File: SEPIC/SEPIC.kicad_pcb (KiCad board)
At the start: 2 copper layers, 49 x 71.5 mm, 24 parts, among them J1 Screw Terminal, J2 Barrel Jack, J3 Pin Header, J4 Screw Terminal, Q1 IRF520N, U1 HCPL-3120

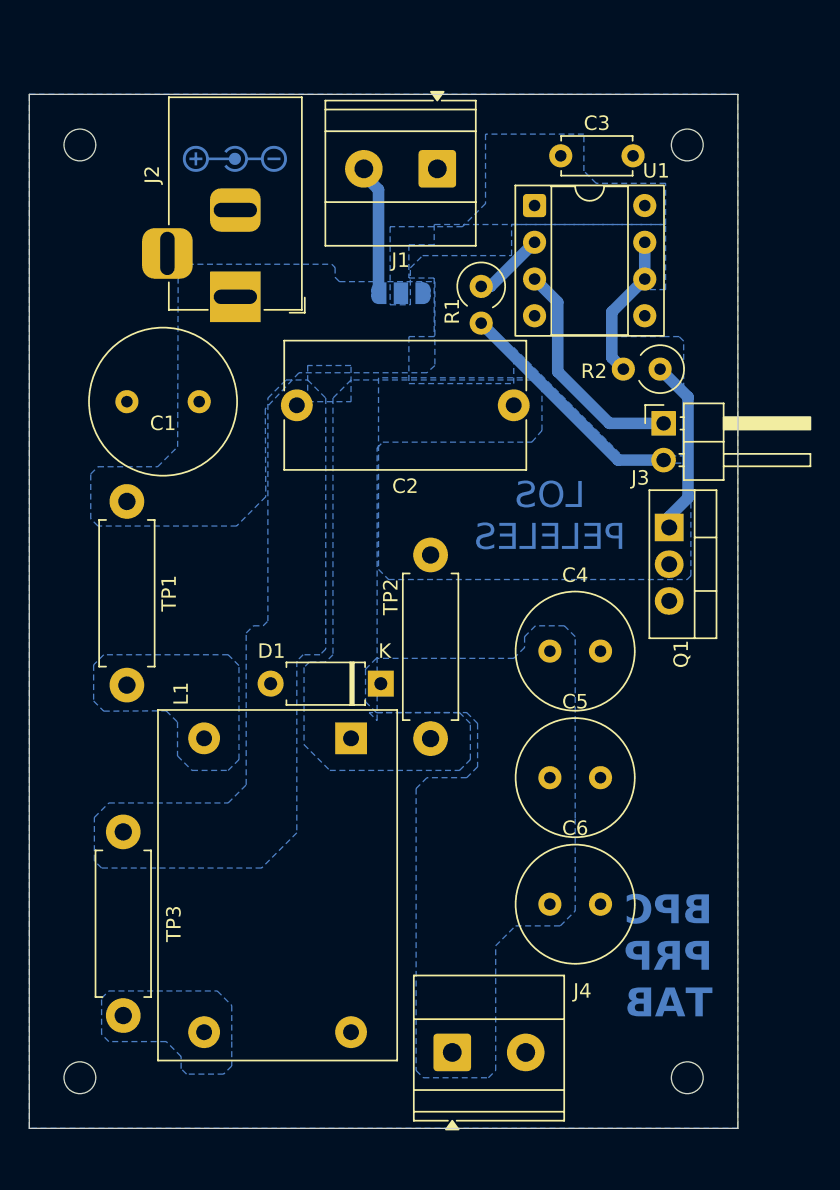
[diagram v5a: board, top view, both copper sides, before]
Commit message: Cambiar tamaño perforaciones
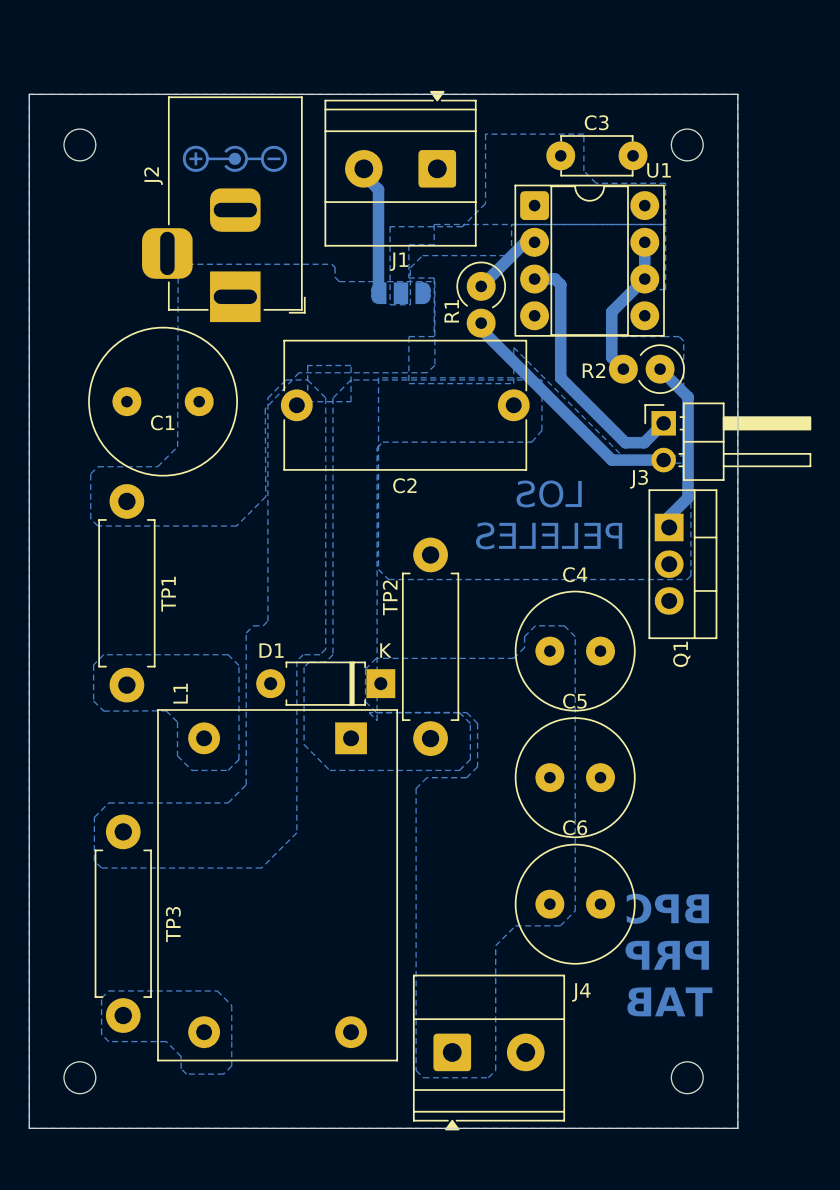
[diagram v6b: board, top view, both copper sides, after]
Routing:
- net Net-(J3-Pin_1): track 15.9 -> 17.9 mm
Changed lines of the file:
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@@
 		(tenting front back)
 		(pcbplotparams
-			(layerselection 0x00000000_00000000_55555555_55555554)
+			(layerselection 0x00000000_00000000_55555555_57555554)
 			(plot_on_all_layers_selection 0x00000000_00000000_00000000_00000000)
 			(disableapertmacros no)
@@
 		(pad "1" thru_hole circle
 			(at 0 0)
-			(size 1.6 1.6)
+			(size 2 2)
 			(drill 0.8)
 			(layers "*.Cu" "*.Mask")
@@
 		(pad "2" thru_hole circle
 			(at 3.5 0)
-			(size 1.6 1.6)
+			(size 2 2)
 			(drill 0.8)
 			(layers "*.Cu" "*.Mask")
@@
 		(pad "1" thru_hole circle
 			(at 0 0)
-			(size 1.6 1.6)
+			(size 2 2)
 			(drill 0.8)
 			(layers "*.Cu" "*.Mask")
@@
 		(pad "2" thru_hole circle
 			(at 3.5 0)
-			(size 1.6 1.6)
+			(size 2 2)
 			(drill 0.8)
 			(layers "*.Cu" "*.Mask")
@@
 		(pad "1" thru_hole circle
 			(at 0 0 180)
-			(size 1.6 1.6)
+			(size 2 2)
 			(drill 0.8)
 			(layers "*.Cu" "*.Mask")
@@
 		(pad "2" thru_hole circle
 			(at 5 0 180)
-			(size 1.6 1.6)
+			(size 2 2)
 			(drill 0.8)
 			(layers "*.Cu" "*.Mask")
@@
 		(pad "1" thru_hole circle
 			(at 0 0 270)
-			(size 1.6 1.6)
+			(size 2 2)
 			(drill 0.8)
 			(layers "*.Cu" "*.Mask")
@@
 			(pintype "passive")
 		)
-		(pad "2" thru_hole oval
+		(pad "2" thru_hole circle
 			(at 2.54 0 270)
-			(size 1.6 1.6)
+			(size 2 2)
 			(drill 0.8)
 			(layers "*.Cu" "*.Mask")
@@
 		(pad "1" thru_hole circle
 			(at 0 0)
-			(size 1.6 1.6)
+			(size 2 2)
 			(drill 0.8)
 			(layers "*.Cu" "*.Mask")
@@
 		(pad "2" thru_hole circle
 			(at 3.5 0)
-			(size 1.6 1.6)
+			(size 2 2)
 			(drill 0.8)
 			(layers "*.Cu" "*.Mask")
@@
 		(pad "1" thru_hole rect
 			(at 0 0 180)
-			(size 1.8 1.8)
+			(size 2 2)
 			(drill 0.9)
 			(layers "*.Cu" "*.Mask")
@@
 			(pintype "passive")
 		)
-		(pad "2" thru_hole oval
+		(pad "2" thru_hole circle
 			(at 7.62 0 180)
-			(size 1.8 1.8)
+			(size 2 2)
 			(drill 0.9)
 			(layers "*.Cu" "*.Mask")
@@
 		(pad "1" thru_hole circle
 			(at 0 0 180)
-			(size 1.6 1.6)
+			(size 2 2)
 			(drill 0.8)
 			(layers "*.Cu" "*.Mask")
@@
 			(pintype "passive")
 		)
-		(pad "2" thru_hole oval
+		(pad "2" thru_hole circle
 			(at 2.54 0 180)
-			(size 1.6 1.6)
+			(size 2 2)
 			(drill 0.8)
 			(layers "*.Cu" "*.Mask")
@@
 		(pad "1" thru_hole circle
 			(at 0 0)
-			(size 1.6 1.6)
+			(size 2 2)
 			(drill 0.8)
 			(layers "*.Cu" "*.Mask")
@@
 		(pad "2" thru_hole circle
 			(at 5 0)
-			(size 1.6 1.6)
+			(size 2 2)
 			(drill 0.8)
 			(layers "*.Cu" "*.Mask")
@@
 		(tags "THT DIP DIL PDIP 2.54mm 7.62mm 300mil Socket")
 		(property "Reference" "U1"
-			(at 8.41 -2.4 0)
+			(at 8.61 -2.4 0)
 			(layer "F.SilkS")
 			(effects
@@
 		(pad "1" thru_hole roundrect
 			(at 0 0)
-			(size 1.6 1.6)
+			(size 2 2)
 			(drill 0.8)
 			(layers "*.Cu" "*.Mask")
@@
 		(pad "2" thru_hole circle
 			(at 0 2.54)
-			(size 1.6 1.6)
+			(size 2 2)
 			(drill 0.8)
 			(layers "*.Cu" "*.Mask")
@@
 		(pad "3" thru_hole circle
 			(at 0 5.08)
-			(size 1.6 1.6)
+			(size 2 2)
 			(drill 0.8)
 			(layers "*.Cu" "*.Mask")
@@
 		(pad "4" thru_hole circle
 			(at 0 7.62)
-			(size 1.6 1.6)
+			(size 2 2)
 			(drill 0.8)
 			(layers "*.Cu" "*.Mask")
@@
 		(pad "5" thru_hole circle
 			(at 7.62 7.62)
-			(size 1.6 1.6)
+			(size 2 2)
 			(drill 0.8)
 			(layers "*.Cu" "*.Mask")
@@
 		(pad "6" thru_hole circle
 			(at 7.62 5.08)
-			(size 1.6 1.6)
+			(size 2 2)
 			(drill 0.8)
 			(layers "*.Cu" "*.Mask")
@@
 		(pad "7" thru_hole circle
 			(at 7.62 2.54)
-			(size 1.6 1.6)
+			(size 2 2)
 			(drill 0.8)
 			(layers "*.Cu" "*.Mask")
@@
 		(pad "8" thru_hole circle
 			(at 7.62 0)
-			(size 1.6 1.6)
+			(size 2 2)
 			(drill 0.8)
 			(layers "*.Cu" "*.Mask")
@@
 	)
 	(segment
-		(start 72.791 40.621)
-		(end 71.19 39.02)
+		(start 73 45.87153)
+		(end 77.46747 50.339)
+		(width 0.8)
+		(layer "B.Cu")
+		(net 10)
+	)
+	(segment
+		(start 71.19 39.02)
+		(end 72.604213 39.02)
+		(width 0.8)
+		(layer "B.Cu")
+		(net 10)
+	)
+	(segment
+		(start 72.604213 39.02)
+		(end 73 39.415787)
 		(width 0.8)
 		(layer "B.Cu")
@@
 	)
 	(segment
-		(start 80.115 49)
-		(end 76.365844 49)
+		(start 77.46747 50.339)
+		(end 78.776 50.339)
 		(width 0.8)
 		(layer "B.Cu")
@@
 	)
 	(segment
-		(start 72.791 45.425156)
-		(end 72.791 40.621)
+		(start 73 39.415787)
+		(end 73 45.87153)
 		(width 0.8)
 		(layer "B.Cu")
@@
 	)
 	(segment
-		(start 76.365844 49)
-		(end 72.791 45.425156)
+		(start 78.776 50.339)
+		(end 80.115 49)
 		(width 0.8)
 		(layer "B.Cu")
@@
 	)
 	(segment
-		(start 76.97 51.54)
+		(start 76.54 51.54)
 		(end 80.115 51.54)
 		(width 0.8)
@@
 	(segment
 		(start 67.5 42.07)
-		(end 76.97 51.54)
+		(end 67.5 42.5)
+		(width 0.8)
+		(layer "B.Cu")
+		(net 11)
+	)
+	(segment
+		(start 67.5 42.5)
+		(end 76.54 51.54)
 		(width 0.8)
 		(layer "B.Cu")
@@
 	)
 	(segment
-		(start 68.14 39.53)
-		(end 71.19 36.48)
+		(start 71.19 36.48)
+		(end 70.55 36.48)
 		(width 0.8)
 		(layer "B.Cu")
@@
 	)
 	(segment
-		(start 67.5 39.53)
-		(end 68.14 39.53)
+		(start 70.55 36.48)
+		(end 67.5 39.53)
 		(width 0.8)
 		(layer "B.Cu")
@@
 	)
 	(segment
-		(start 76.530001 44.450001)
-		(end 76.530001 41.299999)
+		(start 78.803001 39.02)
+		(end 76.530001 41.293)
 		(width 0.8)
 		(layer "B.Cu")
@@
 	)
 	(segment
-		(start 76.530001 41.299999)
-		(end 78.81 39.02)
+		(start 76.530001 41.293)
+		(end 76.530001 44.450001)
 		(width 0.8)
 		(layer "B.Cu")
@@
 	)
 	(segment
-		(start 77.33 45.25)
-		(end 76.530001 44.450001)
+		(start 78.81 39.02)
+		(end 78.803001 39.02)
+		(width 0.8)
+		(layer "B.Cu")
+		(net 14)
+	)
+	(segment
+		(start 76.530001 44.450001)
+		(end 77.33 45.25)
 		(width 0.8)
 		(layer "B.Cu")

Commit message: Imagenes PCB
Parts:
- C3: renamed from C4; value 10u -> 22u
- C4: renamed from C5; footprint Capacitor_THT:C_Radial_D8.0mm_H11.5mm_P3.50mm -> Capacitor_THT:C_Radial_D6.3mm_H7.0mm_P2.50mm
- C5: renamed from C6; value 10u -> 22u
- moved C4 0.75 mm to (73.0, 73.5)
- renumbered C3 to C6
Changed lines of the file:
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@@
 		(descr "C, Radial series, Radial, pin pitch=3.50mm, diameter=8mm, height=11.5mm, Non-Polar Electrolytic Capacitor")
 		(tags "C Radial series Radial pin pitch 3.50mm diameter 8mm height 11.5mm Non-Polar Electrolytic Capacitor")
-		(property "Reference" "C6"
+		(property "Reference" "C5"
 			(at 1.75 -5.25 0)
 			(layer "F.SilkS")
@@
 			)
 		)
-		(property "Value" "10u"
+		(property "Value" "22u"
 			(at 1.75 5.25 0)
 			(layer "F.Fab")
@@
 		)
 	)
-	(footprint "Capacitor_THT:C_Radial_D8.0mm_H11.5mm_P3.50mm"
+	(footprint "Capacitor_THT:C_Radial_D6.3mm_H7.0mm_P2.50mm"
 		(layer "F.Cu")
-		(at 72.25 73.5)
-		(descr "C, Radial series, Radial, pin pitch=3.50mm, diameter=8mm, height=11.5mm, Non-Polar Electrolytic Capacitor")
-		(tags "C Radial series Radial pin pitch 3.50mm diameter 8mm height 11.5mm Non-Polar Electrolytic Capacitor")
-		(property "Reference" "C5"
-			(at 1.75 -5.25 0)
+		(at 73 73.5)
+		(descr "C, Radial series, Radial, pin pitch=2.50mm, diameter=6.3mm, height=7mm, Non-Polar Electrolytic Capacitor")
+		(tags "C Radial series Radial pin pitch 2.50mm diameter 6.3mm height 7mm Non-Polar Electrolytic Capacitor")
+		(property "Reference" "C4"
+			(at 1.25 -4.4 0)
 			(layer "F.SilkS")
 			(effects
@@
 		)
 		(property "Value" "10u"
-			(at 1.75 5.25 0)
+			(at 1.25 4.4 0)
 			(layer "F.Fab")
 			(effects
@@
 		(attr through_hole)
 		(fp_circle
-			(center 1.75 0)
-			(end 5.87 0)
+			(center 1.25 0)
+			(end 4.52 0)
 			(stroke
 				(width 0.12)
@@
 		)
 		(fp_circle
-			(center 1.75 0)
-			(end 6 0)
+			(center 1.25 0)
+			(end 4.65 0)
 			(stroke
 				(width 0.05)
@@
 		)
 		(fp_circle
-			(center 1.75 0)
-			(end 5.75 0)
+			(center 1.25 0)
+			(end 4.4 0)
 			(stroke
 				(width 0.1)
@@
 		)
 		(fp_text user "${REFERENCE}"
-			(at 1.75 0 0)
+			(at 1.25 0 0)
 			(layer "F.Fab")
 			(effects
@@
 		(pad "1" thru_hole circle
 			(at 0 0)
-			(size 2 2)
+			(size 1.6 1.6)
 			(drill 0.8)
 			(layers "*.Cu" "*.Mask")
@@
 		)
 		(pad "2" thru_hole circle
-			(at 3.5 0)
-			(size 2 2)
+			(at 2.5 0)
+			(size 1.6 1.6)
 			(drill 0.8)
 			(layers "*.Cu" "*.Mask")
@@
 		)
 		(embedded_fonts no)
-		(model "${KICAD9_3DMODEL_DIR}/Capacitor_THT.3dshapes/C_Radial_D8.0mm_H11.5mm_P3.50mm.wrl"
+		(model "${KICAD9_3DMODEL_DIR}/Capacitor_THT.3dshapes/C_Radial_D6.3mm_H7.0mm_P2.50mm.wrl"
 			(offset
 				(xyz 0 0 0)
@@
 		(descr "C, Radial series, Radial, pin pitch=3.50mm, diameter=8mm, height=11.5mm, Non-Polar Electrolytic Capacitor")
 		(tags "C Radial series Radial pin pitch 3.50mm diameter 8mm height 11.5mm Non-Polar Electrolytic Capacitor")
-		(property "Reference" "C4"
+		(property "Reference" "C3"
 			(at 1.75 -5.25 0)
 			(layer "F.SilkS")
@@
 			)
 		)
-		(property "Value" "10u"
+		(property "Value" "22u"
 			(at 1.75 5.25 0)
 			(layer "F.Fab")
@@
 		(descr "C, Disc series, Radial, pin pitch=5.00mm, diameter*width=4.7*2.5mm^2, Capacitor, http://www.vishay.com/docs/45233/krseries.pdf")
 		(tags "C Disc series Radial pin pitch 5.00mm diameter 4.7mm width 2.5mm Capacitor")
-		(property "Reference" "C3"
+		(property "Reference" "C6"
 			(at 2.5 -2.25 0)
 			(layer "F.SilkS")

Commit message: PCB prototipo mejorado
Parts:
- removed JP1: Solder Jumper, Jumper:SolderJumper-3_P1.3mm_Open_RoundedPad1.0x1.5mm
- removed the REF** at (39.8, 29.8)
- removed the REF** at (81.8, 29.8)
- removed the REF** at (39.8, 94.2)
- removed the REF** at (81.8, 94.2)
- removed the TP1 at (43.0, 54.4)
- added REF**: MountingHole_3.2mm_M3, MountingHole:MountingHole_3.2mm_M3, F.Cu at (40.8, 95.5)
- added REF**: MountingHole_3.2mm_M3, MountingHole:MountingHole_3.2mm_M3, F.Cu at (82.8, 95.5)
- added REF**: MountingHole_3.2mm_M3, MountingHole:MountingHole_3.2mm_M3, F.Cu at (40.8, 26.2)
- added REF**: MountingHole_3.2mm_M3, MountingHole:MountingHole_3.2mm_M3, F.Cu at (82.8, 26.2)
- J3: footprint Connector_PinHeader_2.54mm:PinHeader_1x02_P2.54mm_Horizontal -> Connector_PinHeader_2.54mm:PinHeader_1x02_P2.54mm_Vertical
- L1: value 3m -> 2m
- R2: footprint Resistor_THT:R_Axial_DIN0309_L9.0mm_D3.2mm_P2.54mm_Vertical -> Resistor_THT:R_Axial_DIN0309_L9.0mm_D3.2mm_P12.70mm_Horizontal
- TP1: renamed from TP2; footprint Resistor_THT:R_Axial_DIN0411_L9.9mm_D3.6mm_P12.70mm_Horizontal -> Resistor_THT:R_Axial_DIN0411_L9.9mm_D3.6mm_P25.40mm_Horizontal
- TP2: renamed from TP3; footprint Resistor_THT:R_Axial_DIN0411_L9.9mm_D3.6mm_P12.70mm_Horizontal -> Resistor_THT:R_Axial_DIN0411_L9.9mm_D3.6mm_P25.40mm_Horizontal
- moved J3 28.4 mm to (58.7, 30.2), turned to 90 degrees
- moved TP1 20.2 mm to (81.8, 61.1), turned to -90 degrees
- moved J1 19.9 mm to (82.2, 40.3), turned to 90 degrees
- moved TP2 11.2 mm to (42.8, 88.5), turned to 90 degrees
- moved R1 8.65 mm to (59.5, 36.2), turned to 90 degrees
- moved U1 7.91 mm to (63.3, 33.8)
- moved R2 7.83 mm to (74.5, 51.0), turned to 90 degrees
- moved C2 5.50 mm to (69.8, 53.2)
- moved Q1 5.16 mm to (81.8, 51.2)
- moved J2 4.50 mm to (50.5, 35.8)
- moved C6 2.25 mm to (70.8, 30.5), turned to 180 degrees
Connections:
- C2 pad 1: Net-(C2-Pad1) -> Net-(Q1-D)
- J1 pad 2: Net-(J1-Pin_2) -> VCC
- J2 pad 3: (no net) -> unconnected-(J2-MountPin-Pad3)
- L1 pad 1: Net-(C2-Pad1) -> Net-(Q1-D)
- L1 pad 2: Net-(L1-Pad2) -> +24V
- L1 pad 4: GND -> Net-(D1-A)
- Q1 pad 3: GND -> Net-(Q1-S)
- TP1 pad 1: Net-(C2-Pad1) -> Net-(Q1-S)
- TP1 pad 2: Net-(Q1-D) -> GND
- TP2 pad 1: Net-(D1-A) -> Net-(L1-Pad3)
- TP2 pad 2: Net-(L1-Pad3) -> GND
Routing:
- net VCC: track 0.00 -> 15.3 mm
- net Net-(J3-Pin_2): track 16.8 -> 4.18 mm
- net Net-(J1-Pin_2): track 8.59 -> 0.00 mm
- net Net-(Q1-S): track 0.00 -> 4.88 mm
- net PWM: track 12.3 -> 7.41 mm
- net Net-(J3-Pin_1): track 17.9 -> 13.8 mm
- net Net-(R2-Pad2): track 10.0 -> 6.39 mm
- net Net-(U1-A): track 4.95 -> 3.61 mm
- removed copper zone on B.Cu, net Net-(C2-Pad1)
- removed copper zone on B.Cu, net Net-(L1-Pad2)
- removed copper zone on B.Cu, net VCC
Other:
- board size 49 x 71.5 mm -> 51 x 78.2 mm
- board text removed: "LOS PELELES"
